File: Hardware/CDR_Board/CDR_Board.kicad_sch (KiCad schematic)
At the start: 60 parts, among them J1 BLE Friend, J2 nRF24L01, J3 Battery, J4 ADC, J5 USB_C_Receptacle_USB2.0, Q1 DMP2045U, SW1 BOOTSEL, SW2 RESET, U1 W25Q32JVSS, U2 SOT23-5 200mA 3.3V, U3 RP2040, U4 BQ25172, U6 ADXL343, Y1 Crystal

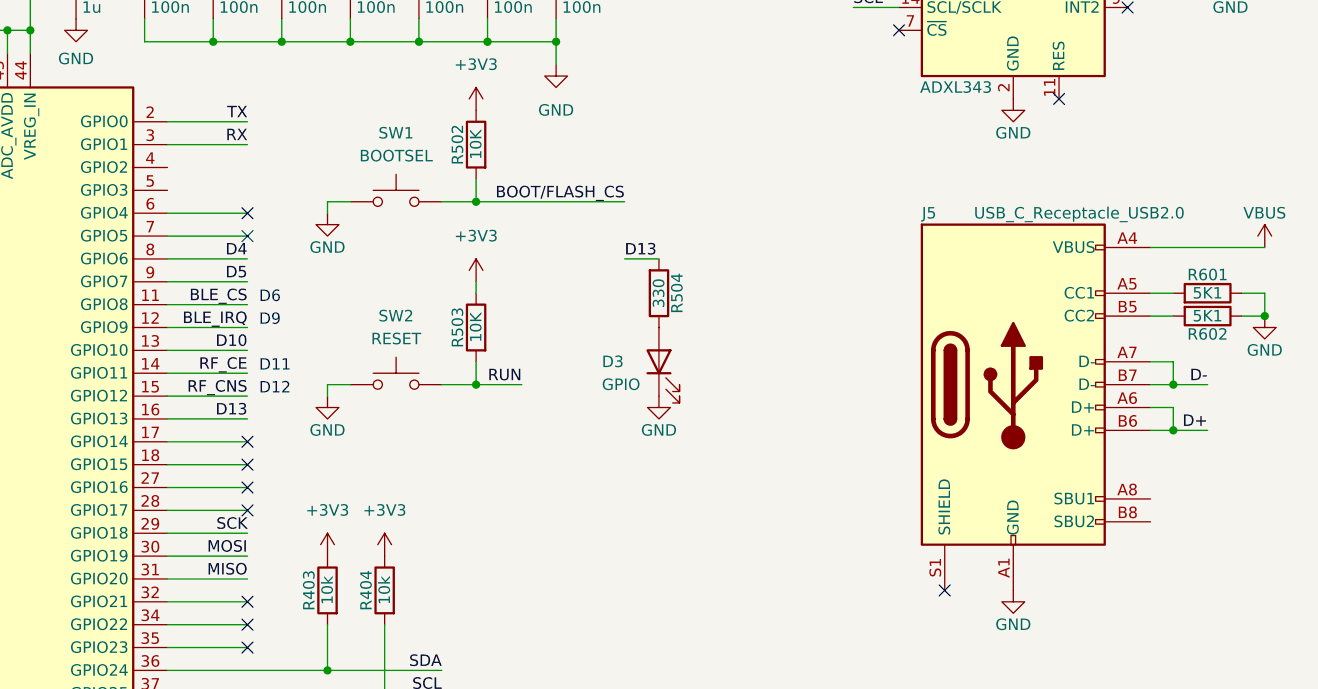
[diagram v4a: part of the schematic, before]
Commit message: Added stitching vias
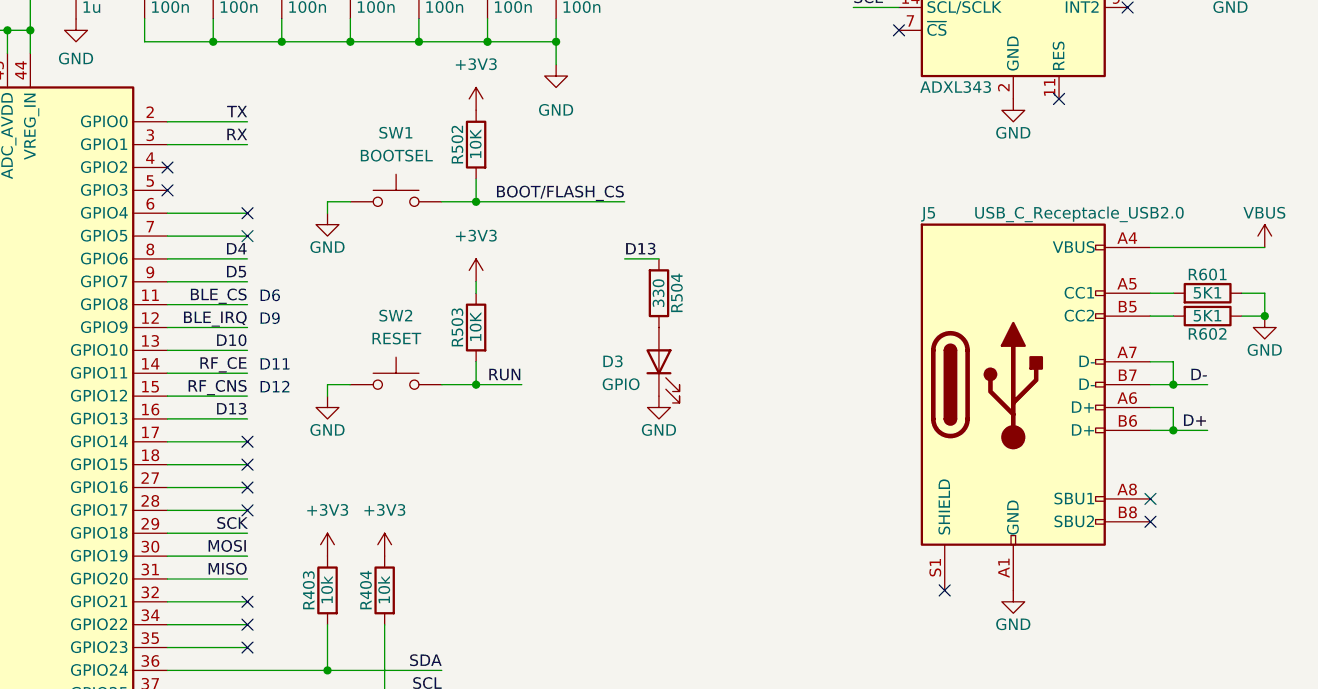
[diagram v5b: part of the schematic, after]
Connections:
- no-connect marks 20 -> 24
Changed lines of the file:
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@@
   )
   (no_connect (at 144.78 160.02))
+  (no_connect (at 135.89 111.76))
+  (no_connect (at 135.89 114.3))
   (no_connect (at 250.19 47.625))
   (no_connect (at 242.57 93.98))
@@
   (no_connect (at 215.9 52.705))
   (no_connect (at 215.9 55.245))
+  (no_connect (at 245.11 148.59))
   (no_connect (at 234.95 104.14))
   (no_connect (at 224.79 78.74))
@@
   (no_connect (at 144.78 116.84))
   (no_connect (at 144.78 142.24))
+  (no_connect (at 245.11 151.13))
   (no_connect (at 222.25 158.75))
   (no_connect (at 144.78 162.56))

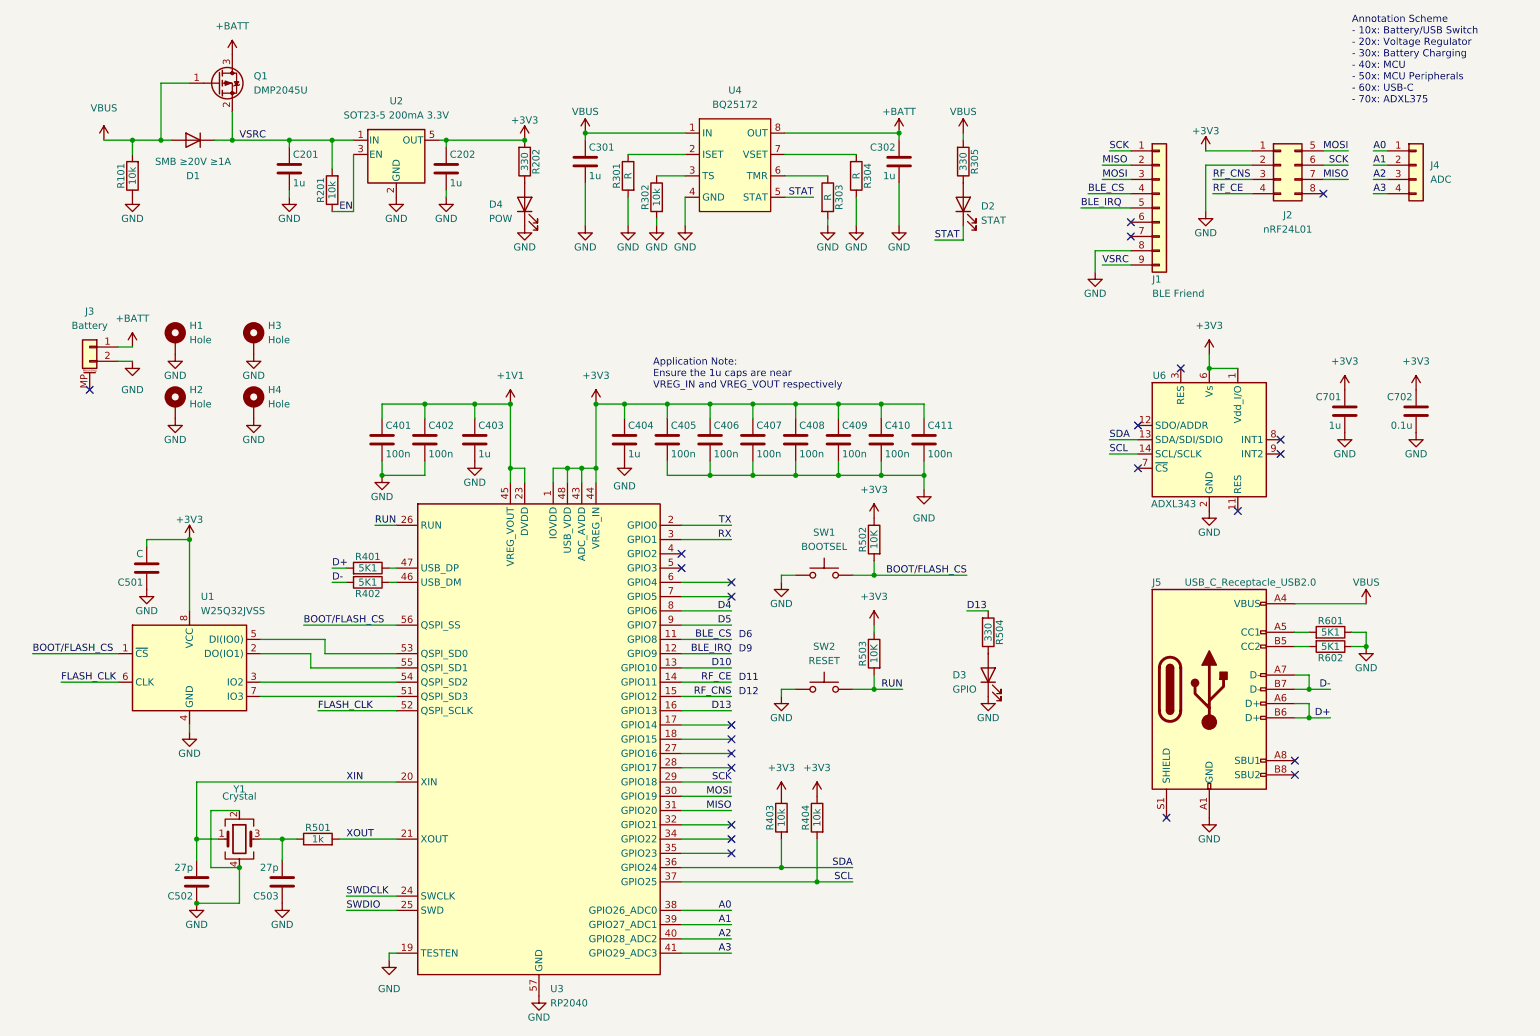
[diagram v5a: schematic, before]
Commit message: Added more stitching vias
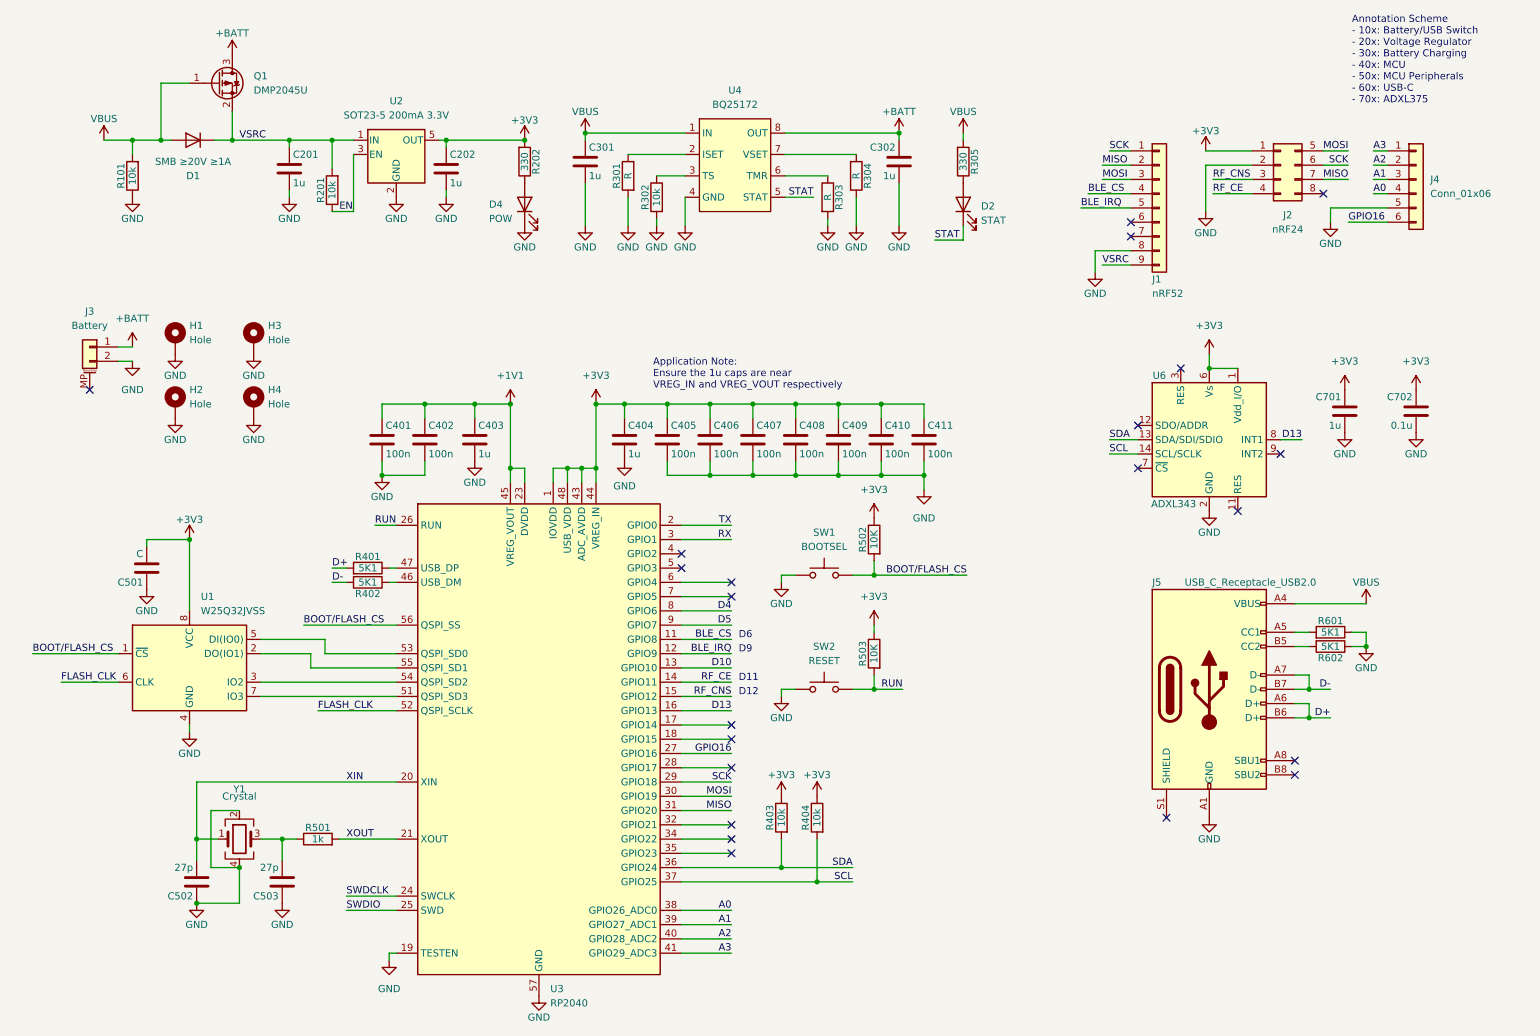
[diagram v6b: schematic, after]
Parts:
- removed D3: GPIO, LED_SMD:LED_0805_2012Metric_Pad1.15x1.40mm_HandSolder, symbol Device:LED
- removed J4: ADC, Connector_PinSocket_2.54mm:PinSocket_1x04_P2.54mm_Vertical, symbol Connector_Generic:Conn_01x04
- removed R504: 330, Resistor_SMD:R_0805_2012Metric_Pad1.20x1.40mm_HandSolder, symbol Device:R
- added J4: Conn_01x06, Connector_PinSocket_2.54mm:PinSocket_1x06_P2.54mm_Vertical, symbol Connector_Generic:Conn_01x06
- J1: value BLE Friend -> nRF52
- J2: value nRF24L01 -> nRF24
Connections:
- net A0: now also J4.4 (Pin_4)
- net A1: now also J4.3 (Pin_3)
- net A2: now also J4.2 (Pin_2)
- net A3: now also J4.1 (Pin_1)
- net D13: now also U6.8 (INT1)
- net GND: now also J4.5 (Pin_5)
- net GPIO16: now reaches U3.27 (GPIO16)
- net GPIO16: now also J4.6 (Pin_6)
- no-connect marks 24 -> 22

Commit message: Finalized PCB v1
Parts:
- added R504: DNF, Resistor_SMD:R_0805_2012Metric_Pad1.20x1.40mm_HandSolder, symbol Device:R
- C501: value C -> 100n
- R502: value 10K -> 1K
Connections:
- net +3V3: now also R504.1; no longer R502.1
- net BOOT/FLASH_CS renamed FLASH_CS
- net FLASH_CS: now also R502.1, R504.2; no longer R502.2, SW1.2
- new net ~{BOOT}: R502.2, SW1.2
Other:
- note added: "Application Note: C701 goes near the Vs pin C702 goes near the Vdd pin"
- moved on the sheet: R502

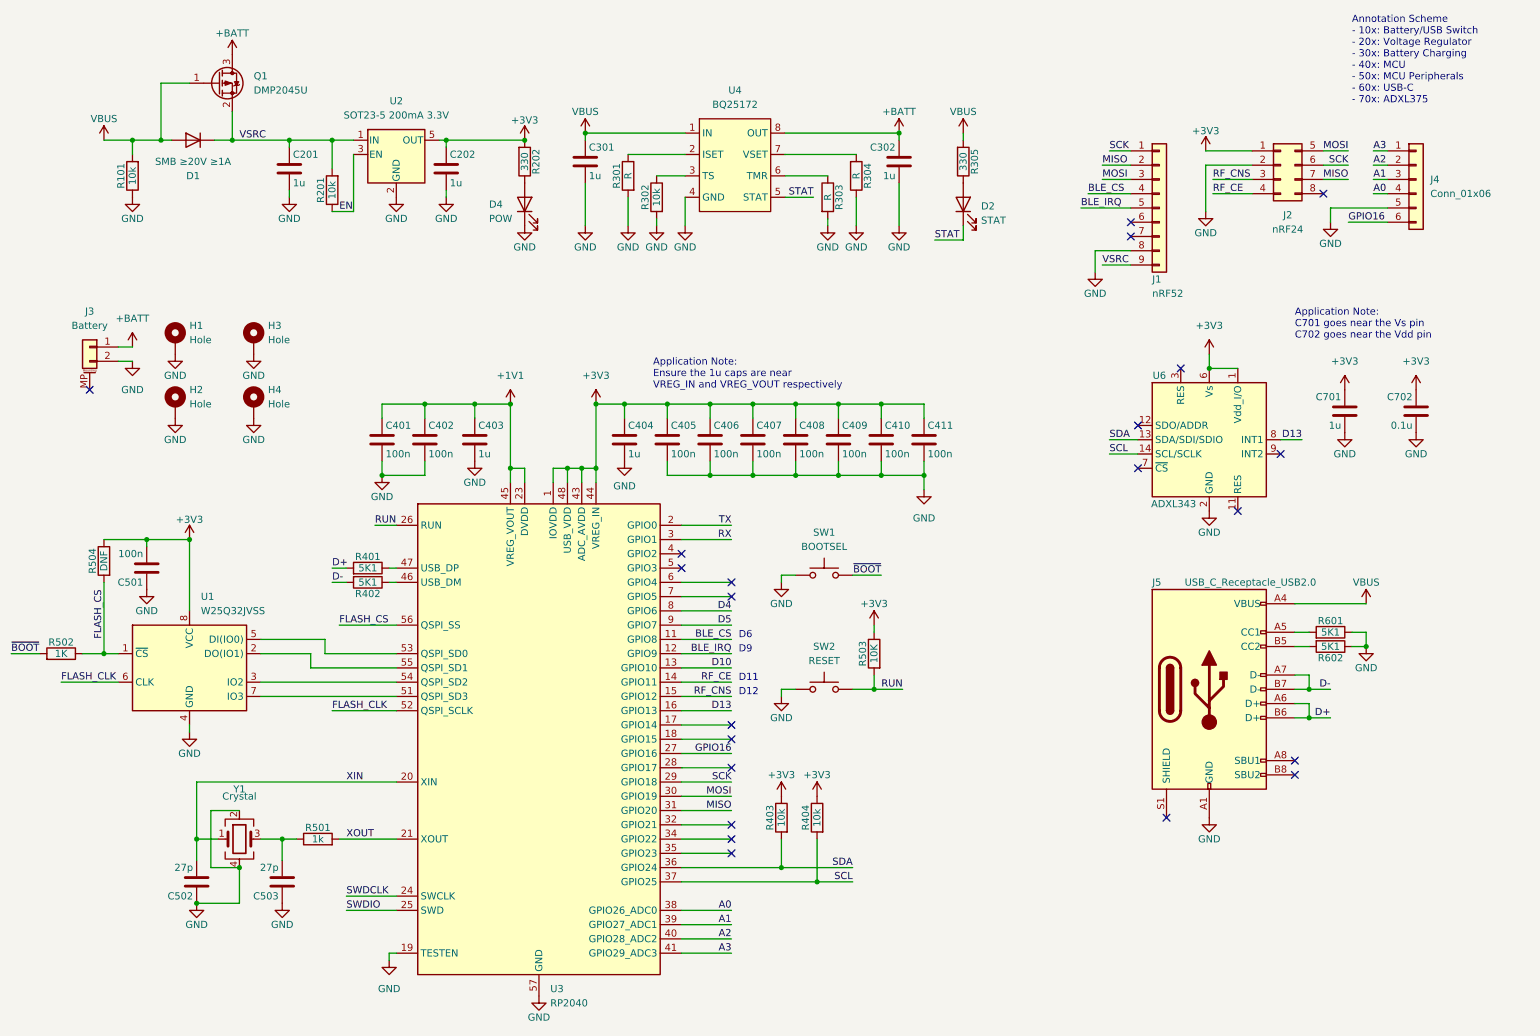
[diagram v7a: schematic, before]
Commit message: Updated helmet PCB
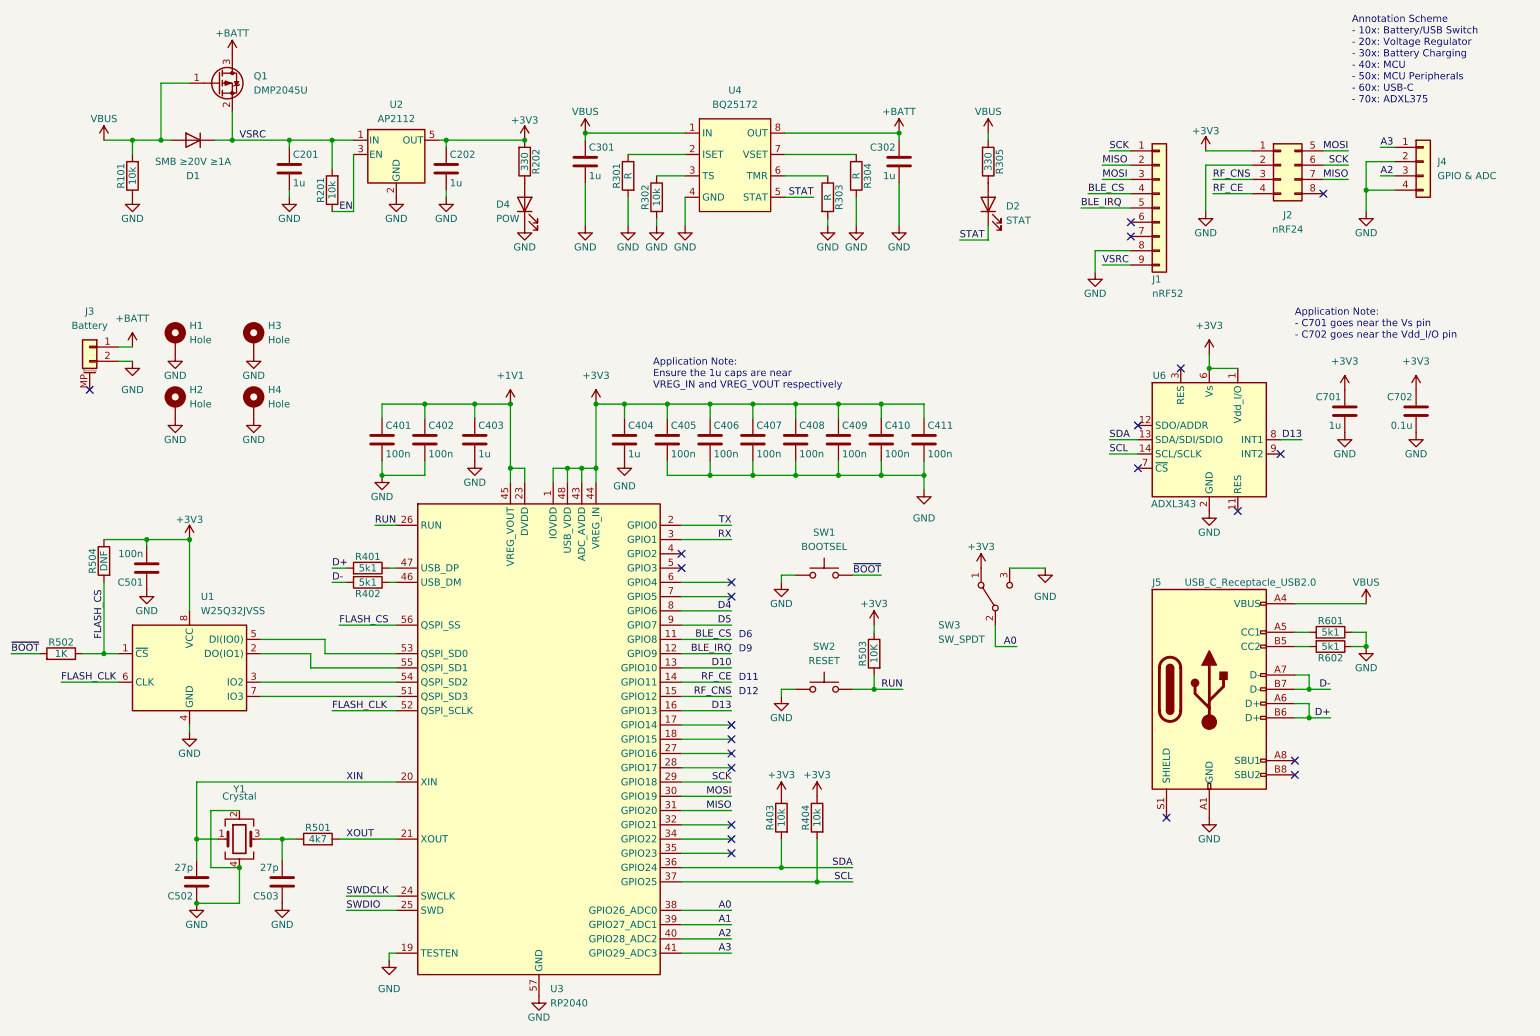
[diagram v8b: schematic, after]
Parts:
- removed J4: Conn_01x06, Connector_PinSocket_2.54mm:PinSocket_1x06_P2.54mm_Vertical, symbol Connector_Generic:Conn_01x06
- added J4: GPIO & ADC, Connector_PinSocket_2.54mm:PinSocket_1x04_P2.54mm_Vertical, symbol Connector_Generic:Conn_01x04
- added SW3: SW_SPDT, SPDT_Footprint:E-Switch-EG1218, symbol Switch:SW_SPDT
- R401, R402, R601, R602: value 5K1 -> 5k1
- R501: value 1k -> 4k7
- U2: value SOT23-5 200mA 3.3V -> AP2112
- Y1: footprint Crystal:Crystal_SMD_SeikoEpson_FA238-4Pin_3.2x2.5mm -> Crystal:Crystal_SMD_0603-4Pin_6.0x3.5mm
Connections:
- net +3V3: now also SW3.1 (A)
- net A0: now also SW3.2 (B)
- net A2: now also J4.3 (Pin_3)
- net A3: now also J4.1 (Pin_1)
- net GND: now also J4.2 (Pin_2), J4.4 (Pin_4), SW3.3 (C)
- net GPIO16: no longer names the net of U3.27 (GPIO16)
- no-connect marks 22 -> 23
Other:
- note added: "Application Note: - C701 goes near the Vs pin - C702 goes near the Vdd_I/O pin"
- note removed: "Application Note: C701 goes near the Vs pin C702 goes near the Vdd pin"
- moved on the sheet: D2, R305
